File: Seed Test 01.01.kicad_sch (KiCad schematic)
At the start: 13 parts, among them J1 Daisy_Seed_Temp, J2 DISP_3_128X64, J3 Micro_SD_Card, SW1 RotaryEncoder_Switch, U1 CS4334

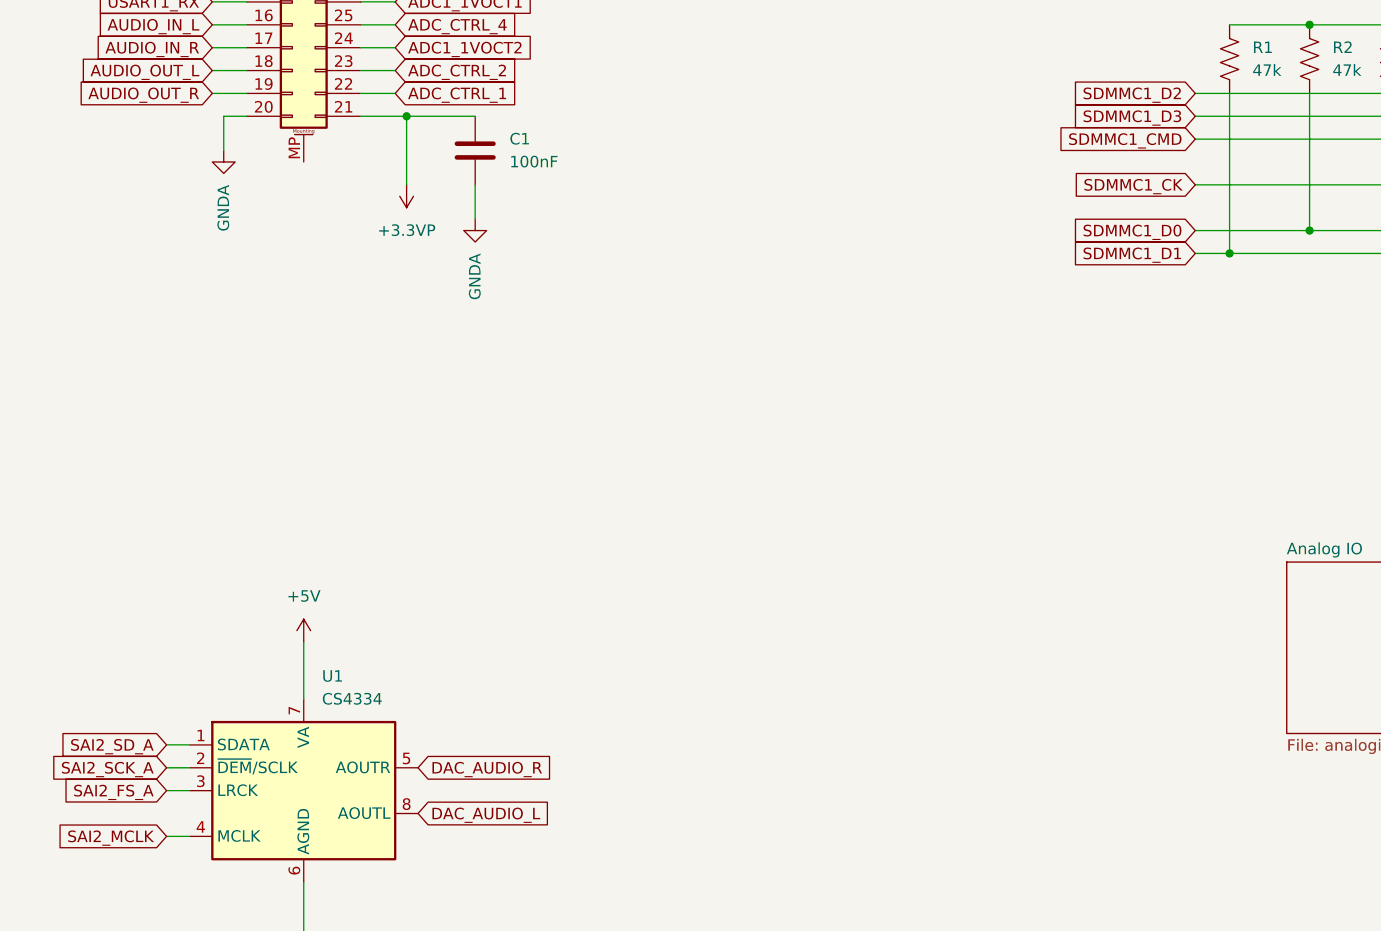
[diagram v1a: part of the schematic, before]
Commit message: Version update
Added DC/DC power block and opAmps for audio input. Redesigned PCB completely moving all components to one side so that it can lay flat.
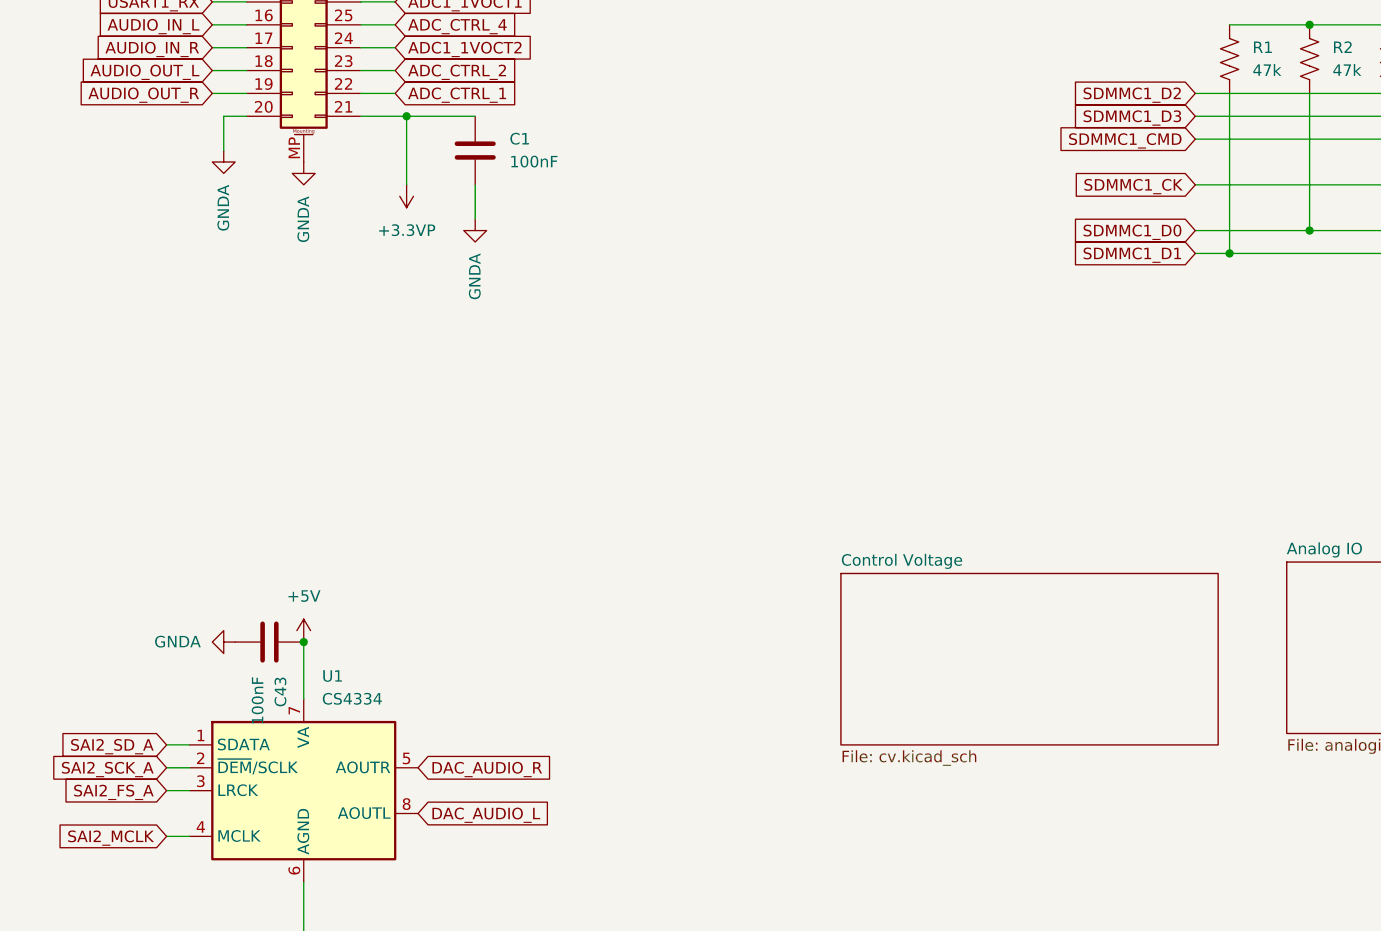
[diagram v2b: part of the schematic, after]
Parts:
- added C43: 100nF, Capacitor_SMD:C_0805_2012Metric, symbol Device:C
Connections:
- net +5V: now also C43.2
- net GNDA: now also J1.MP (MountPin), C43.1
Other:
- added sheet Control Voltage (cv.kicad_sch)

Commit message: Gerber files, BOM updated
Added Gerber files, updated the BOM, and fixed the power sheet to have the correct file name.
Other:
- sheet Power: file untitled.kicad_sch -> power.kicad_sch
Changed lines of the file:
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@@
       (effects (font (size 1.27 1.27)) (justify left bottom))
     )
-    (property "Sheet file" "untitled.kicad_sch" (id 1) (at 229.87 152.9846 0)
+    (property "Sheet file" "power.kicad_sch" (id 1) (at 229.87 152.9846 0)
       (effects (font (size 1.27 1.27)) (justify left top))
     )
@@
       (reference "#PWR0117") (unit 1) (value "+3.3V") (footprint "")
     )
-    (path "/7975bbff-a0ec-44ea-a578-e030126d6fca/b85e9621-f460-4765-8b0c-d3b48fe56e95"
-      (reference "#PWR0118") (unit 1) (value "VEE") (footprint "")
-    )
-    (path "/7975bbff-a0ec-44ea-a578-e030126d6fca/fb42c8a8-fc98-4d42-a1ef-d541a3fcfc47"
-      (reference "#PWR0119") (unit 1) (value "VCC") (footprint "")
-    )
     (path "/70b5bb62-b2b6-4281-a641-07f0ad70152e"
       (reference "#PWR0120") (unit 1) (value "GNDA") (footprint "")
@@
       (reference "#PWR0121") (unit 1) (value "GNDA") (footprint "")
     )
-    (path "/7975bbff-a0ec-44ea-a578-e030126d6fca/a8885972-4d64-4841-885e-56b14f1fb14f"
-      (reference "#PWR0123") (unit 1) (value "-12V") (footprint "")
-    )
-    (path "/7975bbff-a0ec-44ea-a578-e030126d6fca/49e82f45-68f9-49f8-983e-36e7ee8c92a5"
-      (reference "#PWR0124") (unit 1) (value "+12V") (footprint "")
-    )
-    (path "/7975bbff-a0ec-44ea-a578-e030126d6fca/d7ee5c56-3aa2-46f8-b421-c2519e7fa24c"
-      (reference "#PWR0125") (unit 1) (value "GNDA") (footprint "")
-    )
-    (path "/7975bbff-a0ec-44ea-a578-e030126d6fca/7695c83e-cb99-46f5-823b-4f157e3c3f1a"
-      (reference "#PWR0126") (unit 1) (value "GNDA") (footprint "")
-    )
-    (path "/7975bbff-a0ec-44ea-a578-e030126d6fca/1da9a3bf-782f-4a35-bf22-876d6ae3d124"
-      (reference "#PWR0127") (unit 1) (value "+3.3V") (footprint "")
-    )
-    (path "/7975bbff-a0ec-44ea-a578-e030126d6fca/4eab5c4f-21c5-47d9-b6c8-205cf88c6125"
-      (reference "#PWR0128") (unit 1) (value "GNDA") (footprint "")
-    )
-    (path "/7975bbff-a0ec-44ea-a578-e030126d6fca/6091f52c-263a-428c-b94d-b465975cc41a"
-      (reference "#PWR0129") (unit 1) (value "+12V") (footprint "")
-    )
-    (path "/7975bbff-a0ec-44ea-a578-e030126d6fca/b2b789b0-e08f-492f-9a20-6bbf33dc3017"
-      (reference "#PWR0130") (unit 1) (value "GNDA") (footprint "")
-    )
-    (path "/7975bbff-a0ec-44ea-a578-e030126d6fca/a387bfec-16f8-49ec-8b7e-50ddc167a77c"
-      (reference "#PWR0131") (unit 1) (value "+5V") (footprint "")
-    )
-    (path "/7975bbff-a0ec-44ea-a578-e030126d6fca/5e8038ec-8183-4365-8521-2978145b49d2"
-      (reference "#PWR0132") (unit 1) (value "-10V") (footprint "")
-    )
-    (path "/7975bbff-a0ec-44ea-a578-e030126d6fca/c015434c-af21-4836-9cdc-10ee0ef229f8"
-      (reference "#PWR0133") (unit 1) (value "-12V") (footprint "")
-    )
-    (path "/7975bbff-a0ec-44ea-a578-e030126d6fca/782dbb4c-4120-4472-95dc-2e69e8919a42"
-      (reference "#PWR0134") (unit 1) (value "GNDA") (footprint "")
-    )
     (path "/472e7a89-b298-4a75-9ffa-0715f9b55313/66a5f24a-f8e4-4bac-ab28-1fc16c7eb332"
       (reference "#PWR0135") (unit 1) (value "GNDA") (footprint "")
@@
       (reference "#PWR0140") (unit 1) (value "GNDA") (footprint "")
     )
-    (path "/7975bbff-a0ec-44ea-a578-e030126d6fca/24e215c8-7b7b-4531-9947-26c03f02f2ac"
-      (reference "#PWR0141") (unit 1) (value "GNDA") (footprint "")
-    )
     (path "/472e7a89-b298-4a75-9ffa-0715f9b55313/d8dfaa4c-8fe1-450c-81e4-100f3c1e39b9"
       (reference "#PWR0146") (unit 1) (value "GNDA") (footprint "")
@@
       (reference "#PWR0194") (unit 1) (value "GNDA") (footprint "")
     )
+    (path "/7975bbff-a0ec-44ea-a578-e030126d6fca/1da9a3bf-782f-4a35-bf22-876d6ae3d124"
+      (reference "#PWR?") (unit 1) (value "+3.3V") (footprint "")
+    )
+    (path "/7975bbff-a0ec-44ea-a578-e030126d6fca/24e215c8-7b7b-4531-9947-26c03f02f2ac"
+      (reference "#PWR?") (unit 1) (value "GNDA") (footprint "")
+    )
+    (path "/7975bbff-a0ec-44ea-a578-e030126d6fca/49e82f45-68f9-49f8-983e-36e7ee8c92a5"
+      (reference "#PWR?") (unit 1) (value "+12V") (footprint "")
+    )
+    (path "/7975bbff-a0ec-44ea-a578-e030126d6fca/4eab5c4f-21c5-47d9-b6c8-205cf88c6125"
+      (reference "#PWR?") (unit 1) (value "GNDA") (footprint "")
+    )
+    (path "/7975bbff-a0ec-44ea-a578-e030126d6fca/5e8038ec-8183-4365-8521-2978145b49d2"
+      (reference "#PWR?") (unit 1) (value "-10V") (footprint "")
+    )
+    (path "/7975bbff-a0ec-44ea-a578-e030126d6fca/6091f52c-263a-428c-b94d-b465975cc41a"
+      (reference "#PWR?") (unit 1) (value "+12V") (footprint "")
+    )
+    (path "/7975bbff-a0ec-44ea-a578-e030126d6fca/7695c83e-cb99-46f5-823b-4f157e3c3f1a"
+      (reference "#PWR?") (unit 1) (value "GNDA") (footprint "")
+    )
+    (path "/7975bbff-a0ec-44ea-a578-e030126d6fca/782dbb4c-4120-4472-95dc-2e69e8919a42"
+      (reference "#PWR?") (unit 1) (value "GNDA") (footprint "")
+    )
+    (path "/7975bbff-a0ec-44ea-a578-e030126d6fca/a387bfec-16f8-49ec-8b7e-50ddc167a77c"
+      (reference "#PWR?") (unit 1) (value "+5V") (footprint "")
+    )
+    (path "/7975bbff-a0ec-44ea-a578-e030126d6fca/a8885972-4d64-4841-885e-56b14f1fb14f"
+      (reference "#PWR?") (unit 1) (value "-12V") (footprint "")
+    )
+    (path "/7975bbff-a0ec-44ea-a578-e030126d6fca/b2b789b0-e08f-492f-9a20-6bbf33dc3017"
+      (reference "#PWR?") (unit 1) (value "GNDA") (footprint "")
+    )
+    (path "/7975bbff-a0ec-44ea-a578-e030126d6fca/b85e9621-f460-4765-8b0c-d3b48fe56e95"
+      (reference "#PWR?") (unit 1) (value "VEE") (footprint "")
+    )
+    (path "/7975bbff-a0ec-44ea-a578-e030126d6fca/c015434c-af21-4836-9cdc-10ee0ef229f8"
+      (reference "#PWR?") (unit 1) (value "-12V") (footprint "")
+    )
+    (path "/7975bbff-a0ec-44ea-a578-e030126d6fca/d7ee5c56-3aa2-46f8-b421-c2519e7fa24c"
+      (reference "#PWR?") (unit 1) (value "GNDA") (footprint "")
+    )
+    (path "/7975bbff-a0ec-44ea-a578-e030126d6fca/fb42c8a8-fc98-4d42-a1ef-d541a3fcfc47"
+      (reference "#PWR?") (unit 1) (value "VCC") (footprint "")
+    )
     (path "/58123c78-c81f-4b1c-9b3e-5c2bd4ec2134"
